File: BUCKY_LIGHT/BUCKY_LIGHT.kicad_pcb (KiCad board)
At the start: 2 copper layers, 145 x 130 mm, 118 parts, among them J1 Conn_01x16, J2 Conn_01x02, Q1 Q_Photo_NPN, Q10 Q_Photo_NPN, Q11 Q_Photo_NPN, Q12 Q_Photo_NPN, Q13 Q_Photo_NPN, Q14 Q_Photo_NPN, Q15 Q_Photo_NPN, Q16 Q_Photo_NPN, Q17 Q_Photo_NPN, Q18 Q_Photo_NPN, Q19 Q_Photo_NPN, Q2 Q_Photo_NPN, Q20 Q_Photo_NPN, Q21 Q_Photo_NPN, Q22 Q_Photo_NPN, Q23 Q_Photo_NPN, Q24 Q_Photo_NPN, Q25 Q_Photo_NPN, Q26 Q_Photo_NPN, Q27 Q_Photo_NPN, Q28 Q_Photo_NPN, Q3 Q_Photo_NPN, Q4 Q_Photo_NPN, Q5 Q_Photo_NPN, Q6 Q_Photo_NPN, Q7 Q_Photo_NPN, Q8 Q_Photo_NPN, Q9 Q_Photo_NPN, U1 FRONT, U2 RIGHT, U3 DOWN, U4 LEFT

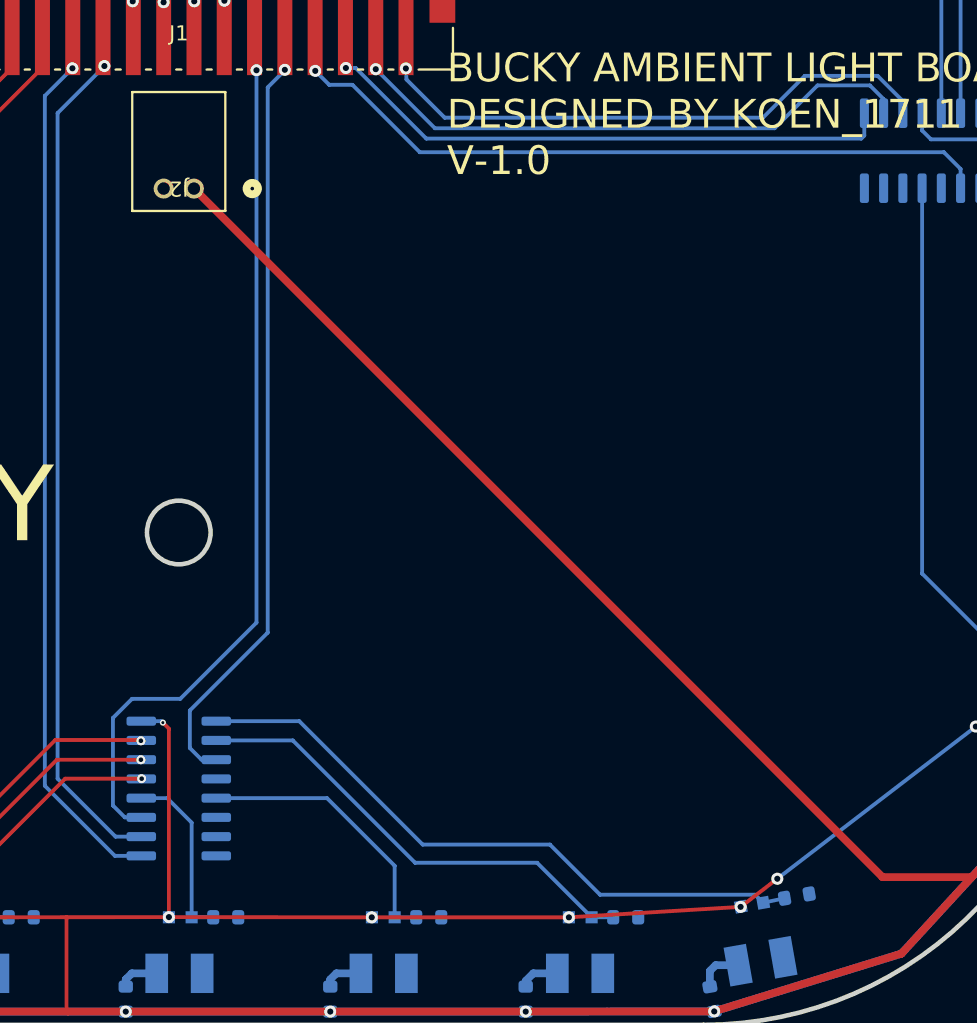
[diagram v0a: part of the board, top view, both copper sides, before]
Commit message: chore: start on ldr instead of Q_Photo_N, interrupt instead of analog multiplexer. And a signal for front,back,left,right
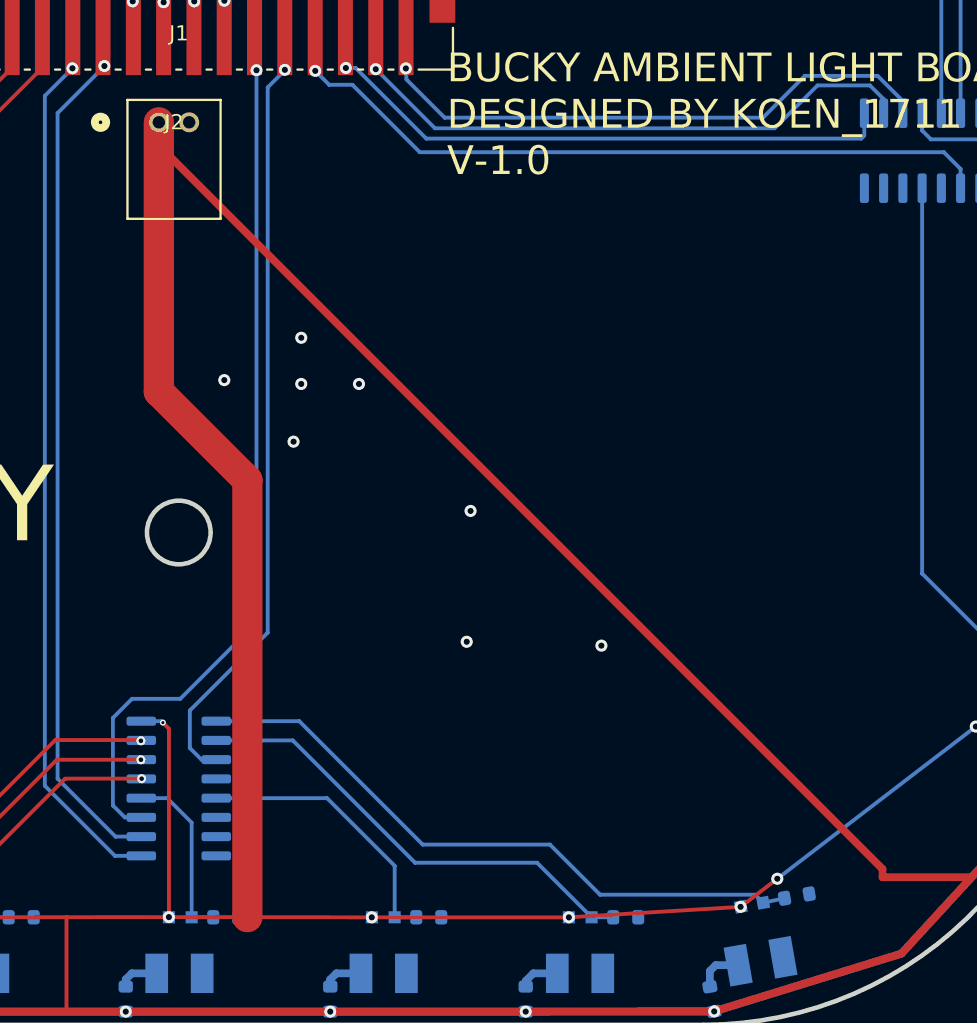
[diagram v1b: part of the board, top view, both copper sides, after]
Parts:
- moved J2 4.95 mm to (142.0, 103.1), turned to 0 degrees
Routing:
- net +5V: track 1404.3 -> 1464.5 mm
- net GND: vias 0 -> 8

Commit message: finish up robot (i think)
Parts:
- removed D10, D11, D12, D13, D14, D15, D16, D17, D18, D19, D2, D20, D21, D22, D23, D24, D25, D26, D27, D28, D3, D4, D5, D6, D7, D8, D9: LED, LED_SMD:LED_PLCC-2
- removed J2: Conn_01x02, BUCKY_LIGHT:BUCKY_POWER_CONN
- removed R34, R41, R42, R43, R44, R49, R50, R51, R52: 10k, Resistor_SMD:R_0603_1608Metric
- removed R38, R40, R45, R46, R47, R48, R53, R54, R55, R56: 90R, Resistor_SMD:R_0603_1608Metric
- removed U1: FRONT, Package_SO:SOIC-16_3.9x9.9mm_P1.27mm
- removed U2: RIGHT, Package_SO:SOIC-16_3.9x9.9mm_P1.27mm
- removed U3: DOWN, Package_SO:SOIC-16_3.9x9.9mm_P1.27mm
- removed U4: LEFT, Package_SO:SOIC-16_3.9x9.9mm_P1.27mm
- added IC1: TLV7034RTER, BUCKY_LIGHT:ANALOG_COMP, F.Cu at (162.2, 143.5)
- added IC2: TLV7034RTER, BUCKY_LIGHT:ANALOG_COMP, F.Cu at (121.9, 143.5)
- added IC3: TLV7034RTER, BUCKY_LIGHT:ANALOG_COMP, F.Cu at (95.8, 121.3)
- added IC4: TLV7034RTER, BUCKY_LIGHT:ANALOG_COMP, F.Cu at (94.9, 81.5)
- added IC5: TLV7034RTER, BUCKY_LIGHT:ANALOG_COMP, F.Cu at (125.6, 54.8)
- added IC6: TLV7034RTER, BUCKY_LIGHT:ANALOG_COMP, F.Cu at (162.5, 54.8)
- added IC7: TLV7034RTER, BUCKY_LIGHT:ANALOG_COMP, F.Cu at (189.9, 91.2)
- added IC8: TLV7034RTER, BUCKY_LIGHT:ANALOG_COMP, F.Cu at (189.9, 128.2)
- added L1: LED, LED_SMD:LED_PLCC-2_3.4x3.0mm_AK, B.Cu at (181.4, 158.5)
- added L10: LED, LED_SMD:LED_PLCC-2_3.4x3.0mm_AK, B.Cu at (75.2, 118.4)
- added L11: LED, LED_SMD:LED_PLCC-2_3.4x3.0mm_AK, B.Cu at (73.9, 105.0)
- added L12: LED, LED_SMD:LED_PLCC-2_3.4x3.0mm_AK, B.Cu at (75.2, 91.5)
- added L13: LED, LED_SMD:LED_PLCC-2_3.4x3.0mm_AK, B.Cu at (79.2, 78.5)
- added L14: LED, LED_SMD:LED_PLCC-2_3.4x3.0mm_AK, B.Cu at (85.5, 66.6)
- added L15: LED, LED_SMD:LED_PLCC-2_3.4x3.0mm_AK, B.Cu at (104.6, 47.5)
- added L16: LED, LED_SMD:LED_PLCC-2_3.4x3.0mm_AK, B.Cu at (116.6, 41.1)
- added L17: LED, LED_SMD:LED_PLCC-2_3.4x3.0mm_AK, B.Cu at (129.5, 37.2)
- added L18: LED, LED_SMD:LED_PLCC-2_3.4x3.0mm_AK, B.Cu at (143.0, 35.9)
- added L19: LED, LED_SMD:LED_PLCC-2_3.4x3.0mm_AK, B.Cu at (156.5, 37.2)
- added L2: LED, LED_SMD:LED_PLCC-2_3.4x3.0mm_AK, B.Cu at (169.5, 159.3)
- added L20: LED, LED_SMD:LED_PLCC-2_3.4x3.0mm_AK, B.Cu at (169.4, 41.1)
- added L21: LED, LED_SMD:LED_PLCC-2_3.4x3.0mm_AK, B.Cu at (181.4, 47.5)
- added L22: LED, LED_SMD:LED_PLCC-2_3.4x3.0mm_AK, B.Cu at (200.5, 66.6)
- added L23: LED, LED_SMD:LED_PLCC-2_3.4x3.0mm_AK, B.Cu at (206.8, 78.5)
- added L24: LED, LED_SMD:LED_PLCC-2_3.4x3.0mm_AK, B.Cu at (210.8, 91.5)
- added L25: LED, LED_SMD:LED_PLCC-2_3.4x3.0mm_AK, B.Cu at (212.1, 105.0)
- added L26: LED, LED_SMD:LED_PLCC-2_3.4x3.0mm_AK, B.Cu at (210.8, 118.4)
- added L27: LED, LED_SMD:LED_PLCC-2_3.4x3.0mm_AK, B.Cu at (206.8, 131.4)
- added L28: LED, LED_SMD:LED_PLCC-2_3.4x3.0mm_AK, B.Cu at (200.5, 143.3)
- added L3: LED, LED_SMD:LED_PLCC-2_3.4x3.0mm_AK, B.Cu at (156.5, 159.3)
- added L4: LED, LED_SMD:LED_PLCC-2_3.4x3.0mm_AK, B.Cu at (143.0, 159.3)
- added L5: LED, LED_SMD:LED_PLCC-2_3.4x3.0mm_AK, B.Cu at (129.6, 159.3)
- added L6: LED, LED_SMD:LED_PLCC-2_3.4x3.0mm_AK, B.Cu at (116.6, 159.3)
- added L7: LED, LED_SMD:LED_PLCC-2_3.4x3.0mm_AK, B.Cu at (104.7, 158.5)
- added L8: LED, LED_SMD:LED_PLCC-2_3.4x3.0mm_AK, B.Cu at (85.5, 143.3)
- added L9: LED, LED_SMD:LED_PLCC-2_3.4x3.0mm_AK, B.Cu at (79.2, 131.4)
- added LI1: LED, LED_SMD:LED_0603_1608Metric, B.Cu at (154.7, 143.4)
- added LI10: LED, LED_SMD:LED_0603_1608Metric, B.Cu at (100.1, 124.8)
- added LI11: LED, LED_SMD:LED_0603_1608Metric, B.Cu at (99.7, 116.8)
- added LI12: LED, LED_SMD:LED_0603_1608Metric, B.Cu at (91.5, 79.2)
- added LI13: LED, LED_SMD:LED_0603_1608Metric, B.Cu at (102.0, 83.0)
- added LI14: LED, LED_SMD:LED_0603_1608Metric, B.Cu at (102.0, 81.2)
- added LI15: LED, LED_SMD:LED_0603_1608Metric, B.Cu at (136.9, 52.7)
- added LI16: LED, LED_SMD:LED_0603_1608Metric, B.Cu at (126.1, 61.5)
- added LI17: LED, LED_SMD:LED_0603_1608Metric, B.Cu at (128.2, 59.3)
- added LI18: LED, LED_SMD:LED_0603_1608Metric, B.Cu at (136.9, 55.7)
- added LI19: LED, LED_SMD:LED_0603_1608Metric, B.Cu at (168.4, 53.1)
- added LI2: LED, LED_SMD:LED_0603_1608Metric, B.Cu at (161.7, 136.8)
- added LI20: LED, LED_SMD:LED_0603_1608Metric, B.Cu at (159.7, 59.1)
- added LI21: LED, LED_SMD:LED_0603_1608Metric, B.Cu at (162.7, 59.2)
- added LI22: LED, LED_SMD:LED_0603_1608Metric, B.Cu at (186.8, 97.7)
- added LI23: LED, LED_SMD:LED_0603_1608Metric, B.Cu at (183.9, 90.9)
- added LI24: LED, LED_SMD:LED_0603_1608Metric, B.Cu at (183.8, 93.7)
- added LI25: LED, LED_SMD:LED_0603_1608Metric, B.Cu at (183.3, 96.7)
- added LI26: LED, LED_SMD:LED_0603_1608Metric, B.Cu at (189.2, 134.1)
- added LI27: LED, LED_SMD:LED_0603_1608Metric, B.Cu at (183.8, 127.1)
- added LI28: LED, LED_SMD:LED_0603_1608Metric, B.Cu at (183.8, 129.1)
- added LI3: LED, LED_SMD:LED_0603_1608Metric, B.Cu at (160.0, 138.7)
- added LI4: LED, LED_SMD:LED_0603_1608Metric, B.Cu at (156.0, 141.5)
- added LI5: LED, LED_SMD:LED_0603_1608Metric, B.Cu at (119.3, 146.5)
- added LI6: LED, LED_SMD:LED_0603_1608Metric, B.Cu at (122.2, 138.3)
- added LI7: LED, LED_SMD:LED_0603_1608Metric, B.Cu at (119.7, 138.3)
- added LI8: LED, LED_SMD:LED_0603_1608Metric, B.Cu at (95.5, 113.8)
- added LI9: LED, LED_SMD:LED_0603_1608Metric, B.Cu at (98.6, 127.5)
- added REF1: 3362P-1-103, BUCKY_LIGHT:VAR_RESISTOR, F.Cu at (188.0, 151.2)
- added REF2: 3362P-1-103, BUCKY_LIGHT:VAR_RESISTOR, F.Cu at (100.4, 56.6)
- added REF3: 3362P-1-103, BUCKY_LIGHT:VAR_RESISTOR, F.Cu at (191.3, 61.5)
- added REF4: 3362P-1-103, BUCKY_LIGHT:VAR_RESISTOR, F.Cu at (94.7, 146.8)
- D1: value LED -> D; footprint LED_SMD:LED_PLCC-2 -> LED_SMD:LED_PLCC-2_3.4x3.0mm_AK; moved to F.Cu
- J1: value Conn_01x16 -> LIGHT -> MAIN; footprint BUCKY_LIGHT:BUCKY_LIGHT_POWER -> BUCKY_LIGHT:LIGHT_CONN
- R13, R14, R15, R16, R21, R22, R23, R24, R5, R6, R7, R8: value 90R -> 10k
- R29, R30, R31, R32: value 90R -> 10k; moved to F.Cu
- R33, R35, R36: value 10k -> 20k; moved to F.Cu
- R37, R39: value 90R -> 20k; moved to F.Cu
- moved R39 128.1 mm to (96.5, 138.1), turned to 180 degrees
- moved R23 115.1 mm to (200.5, 78.8), turned to 180 degrees
- moved R22 114.5 mm to (193.8, 68.8), turned to 180 degrees
- moved R29 112.6 mm to (120.7, 151.1), turned to -90 degrees
- moved R24 108.5 mm to (205.3, 90.5), turned to 90 degrees
- moved R21 108.5 mm to (176.5, 49.5), turned to 180 degrees
- moved R28 108.4 mm to (199.2, 138.3), turned to 90 degrees
- moved R27 107.5 mm to (201.9, 127.7), turned to 90 degrees
- moved R25 106.9 mm to (205.6, 103.4), turned to 90 degrees
- moved R26 106.9 mm to (204.4, 115.8), turned to 90 degrees
- moved R33 103.7 mm to (188.2, 144.6), turned to 180 degrees
- moved R35 92.8 mm to (103.5, 58.2), turned to 90 degrees
- moved R30 75.9 mm to (78.7, 88.1), turned to 90 degrees
- moved R18 72.2 mm to (139.6, 39.5), turned to 180 degrees
- moved R15 71.9 mm to (108.0, 52.7), turned to 0 degrees
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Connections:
- net L1 renamed /ANALOG_COMP_FRONT/I1
- net L2 renamed /ANALOG_COMP_FRONT/I2
- net L3 renamed /ANALOG_COMP_FRONT/I3
- net L4 renamed /ANALOG_COMP_FRONT/I4
- D1 pad 1: GND -> +5V
- J1 pad 1: R_A -> Net-(D1-A)
- J1 pad 2: R_S0 -> GND
- J1 pad 3: R_S1 -> /SIG_FRONT
- J1 pad 4: R_S2 -> /SIG_BACK
- J1 pad 5: F_S2 -> /SIG_LEFT
- J1 pad 6: F_S1 -> /SIG_RIGHT
- Q10 pad 2: L10 -> /ANALOG_COMP_RIGHT/I3
- Q11 pad 2: L11 -> /ANALOG_COMP_RIGHT/I4
- Q12 pad 2: L12 -> /ANALOG_COMP_RIGHT/I5
- Q13 pad 2: L13 -> /ANALOG_COMP_RIGHT/I6
- Q14 pad 2: L14 -> /ANALOG_COMP_RIGHT/I7
- Q15 pad 2: L15 -> /ANALOG_COMP_BACK/I1
- Q16 pad 2: L16 -> /ANALOG_COMP_BACK/I2
- Q17 pad 2: L17 -> /ANALOG_COMP_BACK/I3
- Q18 pad 2: L18 -> /ANALOG_COMP_BACK/I4
- Q19 pad 2: L19 -> /ANALOG_COMP_BACK/I5
- Q20 pad 2: L20 -> /ANALOG_COMP_BACK/I6
- Q21 pad 2: L21 -> /ANALOG_COMP_BACK/I7
- Q22 pad 2: L22 -> /ANALOG_COMP_LEFT/I1
- Q23 pad 2: L23 -> /ANALOG_COMP_LEFT/I2
- Q24 pad 2: L24 -> /ANALOG_COMP_LEFT/I3
- Q25 pad 2: L25 -> /ANALOG_COMP_LEFT/I4
- Q26 pad 2: L26 -> /ANALOG_COMP_LEFT/I5
- Q27 pad 2: L27 -> /ANALOG_COMP_LEFT/I6
- Q28 pad 2: L28 -> /ANALOG_COMP_LEFT/I7
- Q5 pad 2: L5 -> /ANALOG_COMP_FRONT/I5
- Q6 pad 2: L6 -> /ANALOG_COMP_FRONT/I6
- Q7 pad 2: L7 -> /ANALOG_COMP_FRONT/I7
- Q8 pad 2: L8 -> /ANALOG_COMP_RIGHT/I1
- Q9 pad 2: L9 -> /ANALOG_COMP_RIGHT/I2
- R10 pad 1: L6 -> /ANALOG_COMP_RIGHT/I3
- R11 pad 1: L7 -> /ANALOG_COMP_RIGHT/I4
- R12 pad 1: L8 -> /ANALOG_COMP_RIGHT/I5
- R13 pad 1: +5V -> /ANALOG_COMP_RIGHT/I6
- R13 pad 2: Net-(D5-A) -> GND
- R14 pad 1: +5V -> /ANALOG_COMP_RIGHT/I7
- R14 pad 2: Net-(D6-A) -> GND
- R15 pad 1: +5V -> /ANALOG_COMP_BACK/I1
- R15 pad 2: Net-(D7-A) -> GND
- R16 pad 1: +5V -> /ANALOG_COMP_BACK/I2
- R16 pad 2: Net-(D8-A) -> GND
- R17 pad 1: L9 -> /ANALOG_COMP_BACK/I3
- R18 pad 1: L10 -> /ANALOG_COMP_BACK/I4
- R19 pad 1: L11 -> /ANALOG_COMP_BACK/I5
- R20 pad 1: L12 -> /ANALOG_COMP_BACK/I6
- R21 pad 1: +5V -> /ANALOG_COMP_BACK/I7
- R21 pad 2: Net-(D9-A) -> GND
- R22 pad 1: +5V -> /ANALOG_COMP_LEFT/I1
- R22 pad 2: Net-(D10-A) -> GND
- R23 pad 1: +5V -> /ANALOG_COMP_LEFT/I2
- R23 pad 2: Net-(D11-A) -> GND
- R24 pad 1: +5V -> /ANALOG_COMP_LEFT/I3
- R24 pad 2: Net-(D12-A) -> GND
- R25 pad 1: L13 -> /ANALOG_COMP_LEFT/I4
- R26 pad 1: L14 -> /ANALOG_COMP_LEFT/I5
- R27 pad 1: L15 -> /ANALOG_COMP_LEFT/I6
- R28 pad 1: L16 -> /ANALOG_COMP_LEFT/I7
- R33 pad 1: L17 -> +5V
- R33 pad 2: GND -> /TRES_FRONT_I
- R35 pad 1: L19 -> +5V
- R35 pad 2: GND -> /TRES_BACK_I
- R36 pad 1: L20 -> +5V
- R36 pad 2: GND -> /TRES_BACK
- R37 pad 2: Net-(D17-A) -> /TRES_LEFT_I
- R39 pad 2: Net-(D19-A) -> /TRES_RIGHT_I
- R5 pad 1: +5V -> /ANALOG_COMP_FRONT/I5
- R5 pad 2: Net-(D1-A) -> GND
- R6 pad 1: +5V -> /ANALOG_COMP_FRONT/I6
- R6 pad 2: Net-(D2-A) -> GND
- R7 pad 1: +5V -> /ANALOG_COMP_FRONT/I7
- R7 pad 2: Net-(D3-A) -> GND
- R8 pad 1: +5V -> /ANALOG_COMP_RIGHT/I1
- R8 pad 2: Net-(D4-A) -> GND
- R9 pad 1: L5 -> /ANALOG_COMP_RIGHT/I2
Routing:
- net +5V: track 1464.5 -> 715.6 mm, vias 60 -> 30
- net /SIG_FRONT: track 0.00 -> 104.9 mm, vias 0 -> 9
- net /SIG_RIGHT: track 0.00 -> 103.0 mm, vias 0 -> 7
- net /SIG_BACK: track 0.00 -> 97.6 mm, vias 0 -> 7
- net /TRES_LEFT_I: track 0.00 -> 95.0 mm, vias 0 -> 8
- net /SIG_LEFT: track 0.00 -> 94.8 mm, vias 0 -> 8
- net /TRES_FRONT_I: track 0.00 -> 93.3 mm, vias 0 -> 8
- net /TRES_RIGHT_I: track 0.00 -> 93.1 mm, vias 0 -> 11
- net /TRES_BACK_I: track 0.00 -> 88.3 mm, vias 0 -> 9
- net Net-(L15-A): track 2.50 -> 89.9 mm, vias 0 -> 7
- net Net-(L22-A): track 3.20 -> 90.2 mm, vias 0 -> 7
- net Net-(L10-A): track 2.94 -> 89.8 mm, vias 0 -> 7
- net Net-(L1-A): track 2.66 -> 86.1 mm, vias 0 -> 7
- net F_S0: track 56.8 -> 0.00 mm, vias 1 -> 0
- net F_S2: track 56.6 -> 0.00 mm, vias 1 -> 0
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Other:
- board text removed: "i see the light!"
- board text removed: "if you didn't notice, i am upside down"

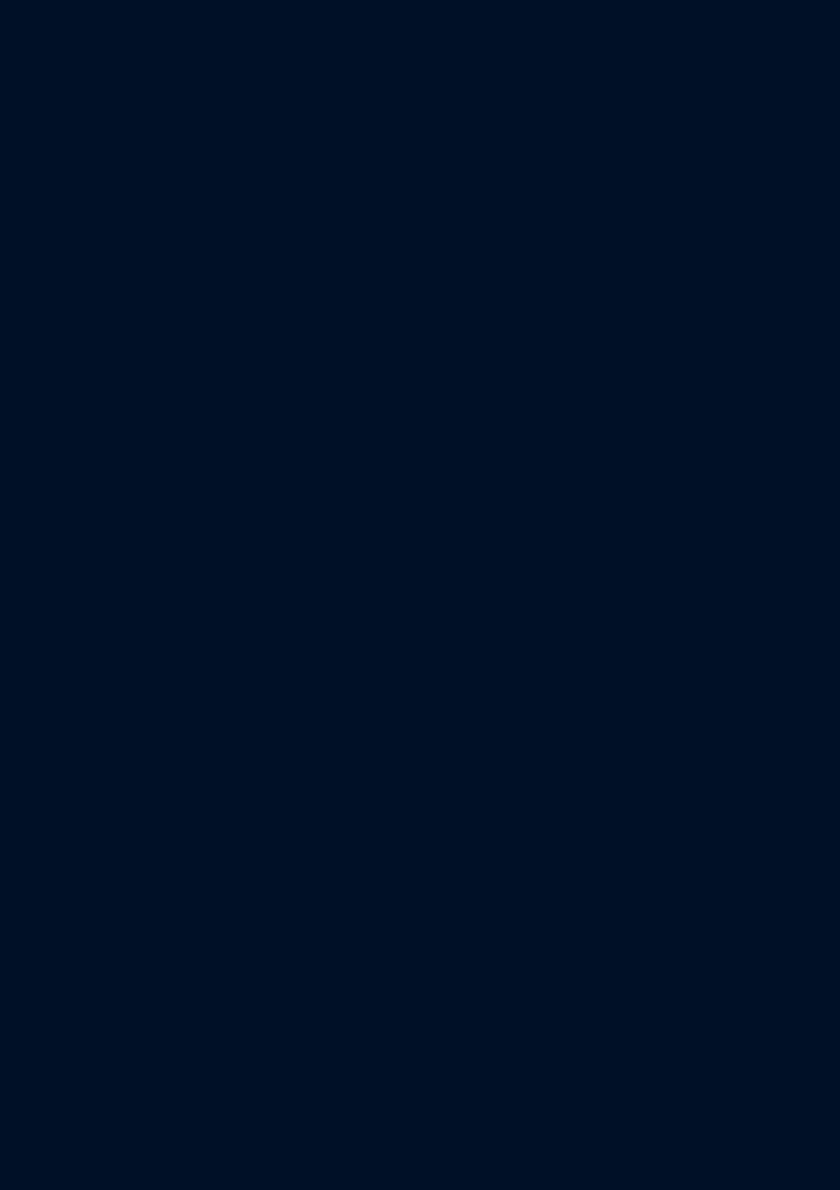
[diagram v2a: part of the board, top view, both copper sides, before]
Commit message: chore: convert 2 layer DRIVE -> 4 layer
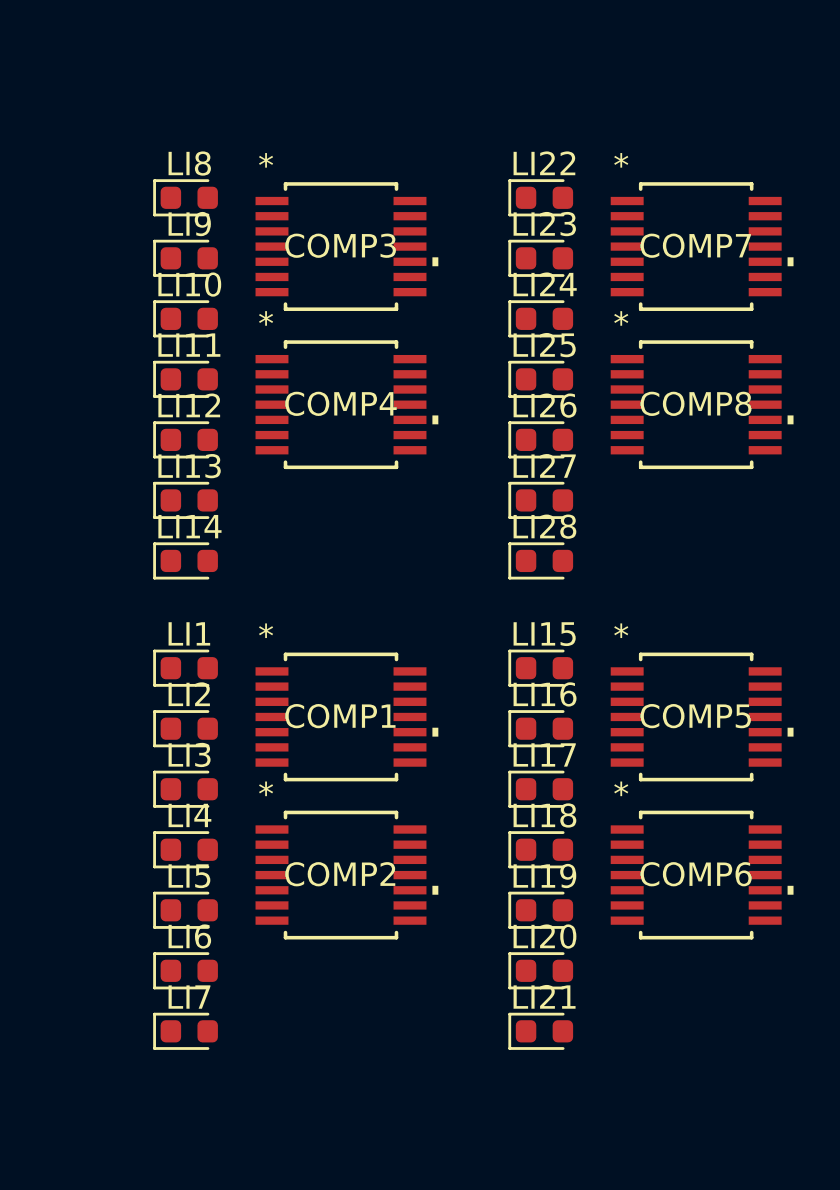
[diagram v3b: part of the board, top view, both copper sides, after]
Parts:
- added COMP1: PTLV7034PWR, BUCKY_LIGHT:ANALOG_COMP, F.Cu at (252.4, 136.8)
- added COMP2: PTLV7034PWR, BUCKY_LIGHT:ANALOG_COMP, F.Cu at (252.4, 143.6)
- added COMP3: PTLV7034PWR, BUCKY_LIGHT:ANALOG_COMP, F.Cu at (252.4, 116.7)
- added COMP4: PTLV7034PWR, BUCKY_LIGHT:ANALOG_COMP, F.Cu at (252.4, 123.4)
- added COMP5: PTLV7034PWR, BUCKY_LIGHT:ANALOG_COMP, F.Cu at (267.6, 136.8)
- added COMP6: PTLV7034PWR, BUCKY_LIGHT:ANALOG_COMP, F.Cu at (267.6, 143.6)
- added COMP7: PTLV7034PWR, BUCKY_LIGHT:ANALOG_COMP, F.Cu at (267.6, 116.7)
- added COMP8: PTLV7034PWR, BUCKY_LIGHT:ANALOG_COMP, F.Cu at (267.6, 123.4)
- added LI1: LED, LED_SMD:LED_0603_1608Metric, F.Cu at (245.9, 134.7)
- added LI10: LED, LED_SMD:LED_0603_1608Metric, F.Cu at (245.9, 119.8)
- added LI11: LED, LED_SMD:LED_0603_1608Metric, F.Cu at (245.9, 122.4)
- added LI12: LED, LED_SMD:LED_0603_1608Metric, F.Cu at (245.9, 124.9)
- added LI13: LED, LED_SMD:LED_0603_1608Metric, F.Cu at (245.9, 127.5)
- added LI14: LED, LED_SMD:LED_0603_1608Metric, F.Cu at (245.9, 130.1)
- added LI15: LED, LED_SMD:LED_0603_1608Metric, F.Cu at (261.1, 134.7)
- added LI16: LED, LED_SMD:LED_0603_1608Metric, F.Cu at (261.1, 137.3)
- added LI17: LED, LED_SMD:LED_0603_1608Metric, F.Cu at (261.1, 139.9)
- added LI18: LED, LED_SMD:LED_0603_1608Metric, F.Cu at (261.1, 142.5)
- added LI19: LED, LED_SMD:LED_0603_1608Metric, F.Cu at (261.1, 145.1)
- added LI2: LED, LED_SMD:LED_0603_1608Metric, F.Cu at (245.9, 137.3)
- added LI20: LED, LED_SMD:LED_0603_1608Metric, F.Cu at (261.1, 147.7)
- added LI21: LED, LED_SMD:LED_0603_1608Metric, F.Cu at (261.1, 150.3)
- added LI22: LED, LED_SMD:LED_0603_1608Metric, F.Cu at (261.1, 114.6)
- added LI23: LED, LED_SMD:LED_0603_1608Metric, F.Cu at (261.1, 117.2)
- added LI24: LED, LED_SMD:LED_0603_1608Metric, F.Cu at (261.1, 119.8)
- added LI25: LED, LED_SMD:LED_0603_1608Metric, F.Cu at (261.1, 122.4)
- added LI26: LED, LED_SMD:LED_0603_1608Metric, F.Cu at (261.1, 124.9)
- added LI27: LED, LED_SMD:LED_0603_1608Metric, F.Cu at (261.1, 127.5)
- added LI28: LED, LED_SMD:LED_0603_1608Metric, F.Cu at (261.1, 130.1)
- added LI3: LED, LED_SMD:LED_0603_1608Metric, F.Cu at (245.9, 139.9)
- added LI4: LED, LED_SMD:LED_0603_1608Metric, F.Cu at (245.9, 142.5)
- added LI5: LED, LED_SMD:LED_0603_1608Metric, F.Cu at (245.9, 145.1)
- added LI6: LED, LED_SMD:LED_0603_1608Metric, F.Cu at (245.9, 147.7)
- added LI7: LED, LED_SMD:LED_0603_1608Metric, F.Cu at (245.9, 150.3)
- added LI8: LED, LED_SMD:LED_0603_1608Metric, F.Cu at (245.9, 114.6)
- added LI9: LED, LED_SMD:LED_0603_1608Metric, F.Cu at (245.9, 117.2)
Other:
- copper layers 2 -> 4

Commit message: chore: make all PCBs from 2 layers to 4 layers
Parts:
- removed IC1, IC2, IC3, IC4, IC5, IC6, IC7, IC8: TLV7034RTER, BUCKY_LIGHT:ANALOG_COMP
- removed the LI1 at (154.7, 143.4)
- removed the LI10 at (100.1, 124.8)
- removed the LI11 at (99.7, 116.8)
- removed the LI12 at (91.5, 79.2)
- removed the LI13 at (102.0, 83.0)
- removed the LI14 at (102.0, 81.2)
- removed the LI15 at (136.9, 52.7)
- removed the LI16 at (126.1, 61.5)
- removed the LI17 at (128.2, 59.3)
- removed the LI18 at (136.9, 55.7)
- removed the LI19 at (168.4, 53.1)
- removed the LI2 at (161.7, 136.8)
- removed the LI20 at (159.7, 59.1)
- removed the LI21 at (162.7, 59.2)
- removed the LI22 at (186.8, 97.7)
- removed the LI23 at (183.9, 90.9)
- removed the LI24 at (183.8, 93.7)
- removed the LI25 at (183.3, 96.7)
- removed the LI26 at (189.2, 134.1)
- removed the LI27 at (183.8, 127.1)
- removed the LI28 at (183.8, 129.1)
- removed the LI3 at (160.0, 138.7)
- removed the LI4 at (156.0, 141.5)
- removed the LI5 at (119.3, 146.5)
- removed the LI6 at (122.2, 138.3)
- removed the LI7 at (119.7, 138.3)
- removed the LI8 at (95.5, 113.8)
- removed the LI9 at (98.6, 127.5)
- removed R36: 20k, Resistor_SMD:R_0603_1608Metric
- COMP1, COMP2, COMP3, COMP4, COMP5, COMP6, COMP7, COMP8: moved to B.Cu
- LI1, LI10, LI11, LI12, LI13, LI14, LI15, LI16, LI17, LI18, LI19, LI2, LI20, LI21, LI22, LI23, LI24, LI25, LI26, LI27, LI28, LI3, LI4, LI5, LI6, LI7, LI8, LI9: footprint LED_SMD:LED_0603_1608Metric -> LED_SMD:LED_0805_2012Metric; moved to B.Cu
- R1, R10, R11, R12, R13, R14, R15, R16, R17, R18, R19, R2, R20, R21, R22, R23, R24, R25, R26, R27, R28, R29, R3, R31, R32, R4, R5, R6, R7, R8, R9: footprint Resistor_SMD:R_0603_1608Metric -> Resistor_SMD:R_0805_2012Metric
- R30, R33, R35, R37, R39: footprint Resistor_SMD:R_0603_1608Metric -> Resistor_SMD:R_0805_2012Metric; moved to B.Cu
- moved COMP4 164.4 mm to (92.8, 84.1), turned to 90 degrees
- moved COMP5 161.8 mm to (131.1, 50.0)
- moved LI16 161.3 mm to (120.3, 58.5), turned to 90 degrees
- moved COMP3 159.1 mm to (93.4, 120.3), turned to 90 degrees
- moved LI17 158.2 mm to (125.4, 58.5), turned to 90 degrees
- moved LI14 152.2 mm to (102.2, 79.8), turned to 180 degrees
- moved LI18 152.1 mm to (134.1, 58.7), turned to 90 degrees
- moved LI15 151.3 mm to (130.3, 58.5), turned to 90 degrees
- moved LI13 150.1 mm to (100.5, 90.5), turned to 180 degrees
- moved LI12 148.6 mm to (102.2, 87.0), turned to 180 degrees
- moved LI11 144.2 mm to (101.7, 119.9), turned to 180 degrees
- moved LI10 144.2 mm to (101.7, 116.5), turned to 180 degrees
- moved LI8 140.7 mm to (105.3, 120.8), turned to -90 degrees
- moved COMP6 138.9 mm to (164.2, 50.8)
- moved LI20 137.7 mm to (156.2, 58.5), turned to 90 degrees
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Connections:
- LI1 pad 1: Net-(LI1-K) -> /SIG_FRONT
- LI10 pad 1: Net-(LI10-K) -> /SIG_RIGHT
- LI11 pad 1: Net-(LI10-K) -> /SIG_RIGHT
- LI15 pad 1: Net-(LI15-K) -> /SIG_BACK
- LI16 pad 1: Net-(LI15-K) -> /SIG_BACK
- LI17 pad 1: Net-(LI15-K) -> /SIG_BACK
- LI18 pad 1: Net-(LI15-K) -> /SIG_BACK
- LI2 pad 1: Net-(LI1-K) -> /SIG_FRONT
- LI22 pad 1: Net-(LI22-K) -> /SIG_LEFT
- LI23 pad 1: Net-(LI22-K) -> /SIG_LEFT
- LI24 pad 1: Net-(LI22-K) -> /SIG_LEFT
- LI25 pad 1: Net-(LI22-K) -> /SIG_LEFT
- LI3 pad 1: Net-(LI1-K) -> /SIG_FRONT
- LI4 pad 1: Net-(LI1-K) -> /SIG_FRONT
- LI8 pad 1: Net-(LI10-K) -> /SIG_RIGHT
- LI9 pad 1: Net-(LI10-K) -> /SIG_RIGHT
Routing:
- net +5V: track 715.6 -> 577.3 mm, vias 30 -> 44
- net /TRES_LEFT_I: track 95.0 -> 71.8 mm, vias 8 -> 0
- net Net-(COMP3-OUT_B): track 0.00 -> 21.8 mm, vias 0 -> 2
- net /SIG_FRONT: track 104.9 -> 83.3 mm, vias 9 -> 0
- net /ANALOG_COMP_LEFT/I7: track 17.5 -> 38.7 mm, vias 1 -> 2
- net /SIG_RIGHT: track 103.0 -> 83.9 mm, vias 7 -> 0
- net Net-(COMP5-OUT_B): track 0.00 -> 15.6 mm, vias 0 -> 2
- net Net-(COMP5-OUT_C): track 0.00 -> 15.5 mm, vias 0 -> 3
- net Net-(COMP8-OUT_A): track 0.00 -> 15.4 mm, vias 0 -> 2
- net Net-(COMP6-OUT_B): track 0.00 -> 13.9 mm, vias 0 -> 3
- net Net-(IC7-OUT_D): track 13.5 -> 0.00 mm, vias 1 -> 0
- net Net-(COMP7-OUT_B): track 0.00 -> 13.2 mm, vias 0 -> 2
- net Net-(COMP1-OUT_B): track 0.00 -> 13.2 mm, vias 0 -> 2
- net Net-(IC5-OUT_D): track 12.9 -> 0.00 mm, vias 1 -> 0
- net Net-(IC7-OUT_A): track 12.6 -> 0.00 mm, vias 1 -> 0
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- added copper zone on In1.Cu, net GND
- added copper zone on In2.Cu, net GND
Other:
- board text added: "BUCKY AMBIENT LIGHT BOARD DESIGNED BY KOEN_1711 08-2024 V-1.0"
- board text added: "BUCKY AMBIENT LIGHT BOARD DESIGNED BY KOEN_1711 09-2024 V-1.0"
- board text removed: "BUCKY AMBIENT LIGHT BOARD DESIGNED BY KOEN_1711 01-2023 V-1.0"

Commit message: fix all drc issues
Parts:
- moved R14 5.40 mm to (94.0, 69.2)
- moved R8 5.20 mm to (91.3, 138.9)
- moved D1 4.49 mm to (149.6, 86.7)
- moved R20 1.09 mm to (163.8, 43.8)
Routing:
- net +5V: track 577.3 -> 587.7 mm
- net Net-(D1-A): track 4.91 -> 9.12 mm
- net /ANALOG_COMP_RIGHT/I7: track 13.4 -> 17.4 mm
- net /ANALOG_COMP_FRONT/I2: track 18.7 -> 15.5 mm
- net /ANALOG_COMP_RIGHT/I1: track 22.9 -> 20.7 mm
- net Net-(COMP6-OUT_C): track 11.0 -> 9.57 mm, vias 3 -> 2
- net Net-(COMP6-OUT_B): track 13.9 -> 12.5 mm, vias 3 -> 2
- net Net-(COMP5-OUT_C): track 15.5 -> 14.8 mm, vias 3 -> 2
